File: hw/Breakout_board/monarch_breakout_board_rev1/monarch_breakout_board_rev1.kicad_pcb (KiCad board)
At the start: 2 copper layers, 21 x 21 mm, 19 parts, among them J108 Conn_01x03, J14 5037630491, U2 FDC2214RGHR, U3 INA226AQDGSRQ1, U4 INA226AQDGSRQ1

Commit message: Footprints, Connectors, and Routing
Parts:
- removed J108: Conn_01x03, Connector_PinSocket_2.54mm:PinSocket_1x03_P2.54mm_Vertical
- removed J14: 5037630491, Connector 4 Pin:CONN_5037630000-SD_04_MOL
- added J1: 5037630491, Connector 4 Pin:CONN_5037630000-SD_04_MOL, F.Cu at (91.7, 36.2)
- added J2: 5037630291, Connector 2 Pin:CONN_5037630000-SD_02_MOL, F.Cu at (83.1, 32.2)
- added J3: 5037630291, Connector 2 Pin:CONN_5037630000-SD_02_MOL, F.Cu at (84.7, 49.5)
- added J4: 5037630291, Connector 2 Pin:CONN_5037630000-SD_02_MOL, F.Cu at (76.8, 49.5)
- added J5: 5037630291, Connector 2 Pin:CONN_5037630000-SD_02_MOL, F.Cu at (74.7, 41.9)
- added J6: 5037630291, Connector 2 Pin:CONN_5037630000-SD_02_MOL, F.Cu at (91.7, 45.0)
- added L1: 18uH, Inductor_SMD:L_0805_2012Metric, F.Cu at (111.0, 50.7)
- added L2: 18uH, Inductor_SMD:L_0805_2012Metric, F.Cu at (111.0, 47.1)
- added L5: 18uH, Inductor_SMD:L_0805_2012Metric, F.Cu at (104.8, 52.1)
- added L6: 18uH, Inductor_SMD:L_0805_2012Metric, F.Cu at (108.4, 52.1)
- added TP5: TestPoint, TestPoint:TestPoint_2Pads_Pitch2.54mm_Drill0.8mm, F.Cu at (106.9, 22.6)
- added TP6: TestPoint, TestPoint:TestPoint_2Pads_Pitch2.54mm_Drill0.8mm, F.Cu at (106.9, 25.9)
- added TP7: TestPoint, TestPoint:TestPoint_2Pads_Pitch2.54mm_Drill0.8mm, F.Cu at (106.9, 29.3)
- added TP8: TestPoint, TestPoint:TestPoint_2Pads_Pitch2.54mm_Drill0.8mm, F.Cu at (106.8, 29.5)
- moved C2 58.3 mm to (113.0, 50.5), turned to 90 degrees
- moved C5 54.3 mm to (113.0, 47.2), turned to 90 degrees
- moved C1 50.9 mm to (103.2, 50.2), turned to 180 degrees
- moved C10 49.3 mm to (108.4, 53.8)
- moved C9 48.1 mm to (104.8, 53.8)
- moved C3 48.1 mm to (104.1, 47.9), turned to -90 degrees
- moved R122 44.2 mm to (108.8, 45.8), turned to 180 degrees
- moved C8 44.2 mm to (102.3, 47.9), turned to -90 degrees
- moved R117 43.8 mm to (107.3, 45.3), turned to -90 degrees
- moved C4 43.3 mm to (100.5, 47.8), turned to -90 degrees
- moved U2 26.9 mm to (107.5, 48.8), turned to -90 degrees
- moved D104 17.9 mm to (91.7, 30.4), turned to 180 degrees
- moved R141 16.1 mm to (88.8, 30.4)
- moved R2 12.2 mm to (77.3, 30.6), turned to 0 degrees
- moved R3 8.94 mm to (87.5, 34.5)
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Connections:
- U2 pad 4: unconnected-(U2-ADDR-Pad4) -> GND
- U3 pad 1: unconnected-(U3-A1-Pad1) -> GND
- U3 pad 2: unconnected-(U3-A0-Pad2) -> GND
- U4 pad 1: unconnected-(U4-A1-Pad1) -> GND
- U4 pad 2: unconnected-(U4-A0-Pad2) -> +3.3V
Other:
- board size 21 x 21 mm -> 23 x 23 mm
- board text added: "Look at application circuit in the datasheet... will be much better"

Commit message: Breakout Board History Fix
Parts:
- added H1: MountingHole, MountingHole:MountingHole_2.2mm_M2_DIN965_Pad, F.Cu at (118.0, 32.6)
- added H2: MountingHole, MountingHole:MountingHole_2.2mm_M2_DIN965_Pad, F.Cu at (118.0, 55.5)
- added H3: MountingHole, MountingHole:MountingHole_2.2mm_M2_DIN965_Pad, F.Cu at (96.8, 32.7)
- added H4: MountingHole, MountingHole:MountingHole_2.2mm_M2_DIN965_Pad, F.Cu at (96.5, 55.7)
- added Y1: SiT5000AI-2E-33N0-40, Oscillator:Oscillator_SMD_SiT_PQFN-4Pin_3.2x2.5mm, F.Cu at (102.8, 44.6)
- moved J5 42.8 mm to (117.4, 40.1), turned to -90 degrees
- moved J4 40.6 mm to (117.4, 47.9), turned to -90 degrees
- moved J3 31.7 mm to (111.6, 32.8), turned to 0 degrees
- moved R122 29.5 mm to (81.0, 35.9)
- moved R141 29.2 mm to (110.8, 49.6), turned to 90 degrees
- moved D104 28.3 mm to (112.2, 49.9), turned to 90 degrees
- moved R117 27.7 mm to (82.2, 33.6), turned to 0 degrees
- moved J1 25.8 mm to (109.3, 55.1), turned to 180 degrees
- moved U3 23.4 mm to (100.4, 38.2), turned to 180 degrees
- moved R3 22.8 mm to (65.4, 29.2), turned to 0 degrees
- moved U4 21.2 mm to (101.7, 53.6)
- moved R2 21.2 mm to (56.1, 29.2)
- moved J2 19.3 mm to (96.9, 45.6), turned to 90 degrees
- moved J6 17.2 mm to (103.7, 32.8), turned to 0 degrees
- moved TP5 14.0 mm to (120.4, 18.6)
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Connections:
- C10 pad 1: /Cap3+ -> Cap3+
- C10 pad 2: /Cap4- -> Cap4-
- C2 pad 1: /Cap5+ -> Cap5+
- C2 pad 2: /Cap6- -> Cap6-
- C5 pad 1: /Cap7+ -> Cap7+
- C5 pad 2: /Cap8- -> Cap8-
- C9 pad 1: /Cap1+ -> Cap1+
- C9 pad 2: /Cap2- -> Cap2-
- J1 pad 1: /Connectors/I2C4_SDA -> I2C4_SDA
- J1 pad 2: /Connectors/I2C4_SCL -> I2C4_SCL
- J2 pad 1: /Connectors/Electro1 -> Electro1
- J2 pad 2: /Connectors/Electro2 -> Electro2
- J3 pad 1: /Connectors/Cap5+ -> Cap5+
- J3 pad 2: /Connectors/Cap6- -> Cap6-
- J4 pad 1: /Connectors/Cap1+ -> Cap1+
- J4 pad 2: /Connectors/Cap2- -> Cap2-
- J5 pad 1: /Connectors/Cap3+ -> Cap3+
- J5 pad 2: /Connectors/Cap4- -> Cap4-
- J6 pad 1: /Connectors/Cap7+ -> Cap7+
- J6 pad 2: /Connectors/Cap8- -> Cap8-
- L1 pad 1: /Cap5+ -> Cap5+
- L1 pad 2: /Cap6- -> Cap6-
- L2 pad 1: /Cap7+ -> Cap7+
- L2 pad 2: /Cap8- -> Cap8-
- L5 pad 1: /Cap1+ -> Cap1+
- L5 pad 2: /Cap2- -> Cap2-
- L6 pad 1: /Cap3+ -> Cap3+
- L6 pad 2: /Cap4- -> Cap4-
- R117 pad 2: /I2C4_SDA -> I2C4_SDA
- R122 pad 2: /I2C4_SCL -> I2C4_SCL
- R2 pad 1: /Electro1 -> Electro1
- R3 pad 1: /Electro2 -> Electro2
- TP5 pad 1: /Connectors/I2C4_SCL -> I2C4_SCL
- TP7 pad 1: /Connectors/I2C4_SDA -> I2C4_SDA
- U2 pad 1: /I2C4_SCL -> I2C4_SCL
- U2 pad 10: /Cap2- -> Cap2-
- U2 pad 11: /Cap3+ -> Cap3+
- U2 pad 12: /Cap4- -> Cap4-
- U2 pad 13: /Cap5+ -> Cap5+
- U2 pad 14: /Cap6- -> Cap6-
- U2 pad 15: /Cap7+ -> Cap7+
- U2 pad 16: /Cap8- -> Cap8-
- U2 pad 2: /I2C4_SDA -> I2C4_SDA
- U2 pad 3: unconnected-(U2-CLKIN-Pad3) -> /CLK_40MHz
- U2 pad 9: /Cap1+ -> Cap1+
- U3 pad 10: /Electro1 -> Electro1
- U3 pad 4: /I2C4_SDA -> I2C4_SDA
- U3 pad 5: /I2C4_SCL -> I2C4_SCL
- U3 pad 8: /Electro1 -> Electro1
- U4 pad 10: /Electro2 -> Electro2
- U4 pad 4: /I2C4_SDA -> I2C4_SDA
- U4 pad 5: /I2C4_SCL -> I2C4_SCL
- U4 pad 8: /Electro2 -> Electro2
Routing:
- net Cap1+: track 0.00 -> 8.76 mm
- net Cap5+: track 0.00 -> 8.55 mm
- net Cap8-: track 0.00 -> 7.84 mm
- net Cap2-: track 0.00 -> 7.76 mm
- net Cap6-: track 0.00 -> 7.37 mm
- net Cap7+: track 0.00 -> 7.26 mm
- net Cap4-: track 0.00 -> 7.09 mm
- net Cap3+: track 0.00 -> 6.63 mm
- net +3V3: track 0.00 -> 2.52 mm
- net /CLK_40MHz: track 0.00 -> 2.06 mm
- net +3.3V: track 0.00 -> 1.69 mm
- net Net-(D104-A): track 0.00 -> 1.50 mm
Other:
- board text removed: "Look at application circuit in the datasheet... will be much better"

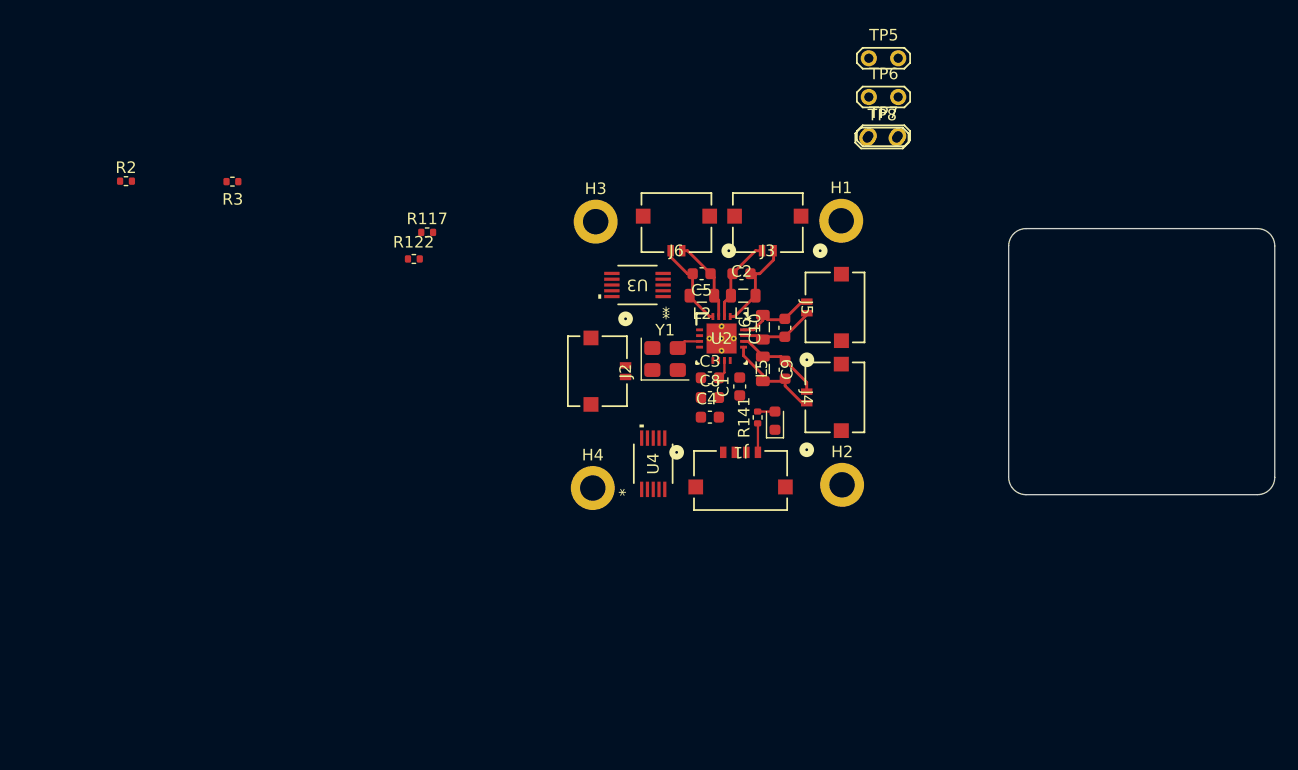
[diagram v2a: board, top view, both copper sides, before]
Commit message: Amplifier Initial Setup / Routing Work
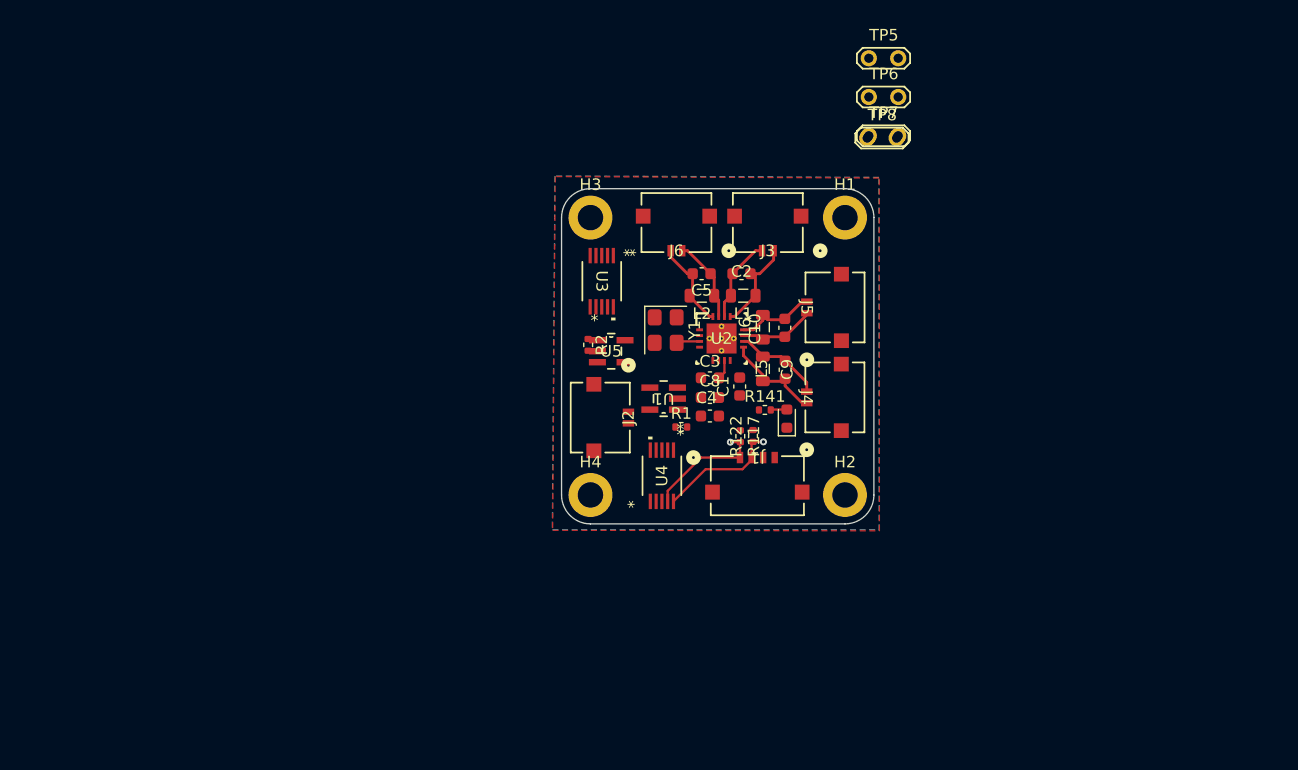
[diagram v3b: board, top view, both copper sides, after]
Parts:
- removed R3: ?, Resistor_SMD:R_0402_1005Metric
- added R1: ?, Resistor_SMD:R_0402_1005Metric, F.Cu at (104.2, 50.5)
- added U1: OPA320AIDBVR, OPA320:DBV5, F.Cu at (102.6, 48.0)
- added U5: OPA320AIDBVR, OPA320:DBV5, F.Cu at (98.1, 43.9)
- moved R2 42.4 mm to (96.1, 43.4), turned to -90 degrees
- moved R122 33.1 mm to (110.3, 51.2), turned to -90 degrees
- moved R117 32.3 mm to (109.2, 51.2), turned to -90 degrees
- moved J2 4.02 mm to (97.1, 49.6)
- moved U3 3.11 mm to (97.3, 37.9), turned to -90 degrees
- moved Y1 2.50 mm to (102.8, 42.1), turned to -90 degrees
- moved J1 1.52 mm to (110.7, 55.5)
- moved U4 1.28 mm to (102.5, 54.7)
- moved D104 1.04 mm to (113.3, 49.7)
- moved H2 0.91 mm to (118.3, 56.3)
- moved R141 0.90 mm to (111.4, 49.0), turned to 0 degrees
- moved H4 0.63 mm to (96.3, 56.3)
- moved H3 0.57 mm to (96.3, 32.4)
- moved H1 0.43 mm to (118.3, 32.4)
- moved C4 0.10 mm to (106.6, 49.5)
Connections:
- R2 pad 1: Electro1 -> unconnected-(R2-Pad1)
- R2 pad 2: GND -> unconnected-(R2-Pad2)
- U3 pad 10: Electro1 -> /VBUS_1
- U3 pad 8: Electro1 -> /VBUS_1
- U3 pad 9: GND -> /VIN-_1
- U4 pad 10: Electro2 -> /VIN+_2
- U4 pad 8: Electro2 -> /VBUS_2
- U4 pad 9: GND -> /VIN-_2
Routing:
- net I2C4_SCL: track 0.00 -> 11.2 mm, vias 0 -> 1
- net I2C4_SDA: track 0.00 -> 10.6 mm, vias 0 -> 1
- net +3V3: track 2.52 -> 0.00 mm
- added copper zone on B.Cu, net GND
- added copper zone on F.Cu, net GND
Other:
- board size 23 x 23 mm -> 27 x 29 mm

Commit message: Final Breakout Board Work
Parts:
- removed C4, C8: 0.01 uF, Capacitor_SMD:C_0603_1608Metric
- removed J1: 5037630491, Connector 4 Pin:CONN_5037630000-SD_04_MOL
- removed R1, R2: ?, Resistor_SMD:R_0402_1005Metric
- removed R117, R122: 4.7k, Resistor_SMD:R_0402_1005Metric
- removed U1, U5: OPA320AIDBVR, OPA320:DBV5
- removed U3, U4: INA226AQDGSRQ1, INA226-Q1:DGS10_TEX
- removed Y1: SiT5000AI-2E-33N0-40, Oscillator:Oscillator_SMD_SiT_PQFN-4Pin_3.2x2.5mm
- J2: value 5037630291 -> 5037630491; footprint Connector 2 Pin:CONN_5037630000-SD_02_MOL -> Connector 4 Pin:CONN_5037630000-SD_04_MOL
- TP5, TP6, TP7, TP8: footprint TestPoint:TestPoint_2Pads_Pitch2.54mm_Drill0.8mm -> TestPoint:TestPoint_Keystone_5000-5004_Miniature
- moved TP5 39.7 mm to (116.5, 58.1), turned to 180 degrees
- moved TP8 35.5 mm to (109.3, 59.3), turned to 180 degrees
- moved TP6 35.5 mm to (109.3, 55.6), turned to 180 degrees
- moved H3 34.0 mm to (109.4, 63.7), turned to 90 degrees
- moved TP7 33.8 mm to (113.1, 58.3), turned to 180 degrees
- moved H4 31.9 mm to (127.4, 63.6), turned to 90 degrees
- moved J2 25.4 mm to (118.7, 63.0), turned to 180 degrees
- moved H2 17.3 mm to (127.4, 41.6), turned to 90 degrees
- moved J6 16.1 mm to (109.7, 47.8), turned to 90 degrees
- moved D104 14.0 mm to (112.6, 63.7)
- moved C1 13.4 mm to (119.0, 56.1)
- moved C3 13.3 mm to (116.4, 55.2)
- moved C10 13.1 mm to (122.8, 50.6)
- moved C2 13.1 mm to (119.1, 45.9)
- moved C9 13.1 mm to (122.9, 54.2)
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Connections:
- C1 pad 2: +3.3V -> +3V3
- C3 pad 2: +3.3V -> +3V3
- J2 pad 1: Electro1 -> I2C4_SDA
- J2 pad 2: Electro2 -> I2C4_SCL
- J2 pad 3: (no net) -> GND
- J2 pad 4: (no net) -> +3V3
- U2 pad 3: /CLK_40MHz -> unconnected-(U2-CLKIN-Pad3)
- U2 pad 7: +3.3V -> +3V3
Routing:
- net +3V3: track 0.00 -> 25.0 mm, vias 0 -> 2
- net I2C4_SDA: track 10.6 -> 14.2 mm
- net Cap8-: track 7.84 -> 5.27 mm
- net /CLK_40MHz: track 2.03 -> 0.00 mm
- net I2C4_SCL: track 11.2 -> 13.2 mm, vias 1 -> 0
- net Cap5+: track 8.55 -> 6.59 mm
- net Cap6-: track 7.37 -> 5.60 mm
- net +3.3V: track 1.69 -> 0.00 mm
- net Cap7+: track 7.26 -> 7.96 mm
- net Cap3+: track 6.63 -> 7.13 mm
- net GND: vias 0 -> 9
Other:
- board size 27 x 29 mm -> 23 x 27.1 mm

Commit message: Breakout Board DONE
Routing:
- net GND: track 0.00 -> 3.49 mm, vias 9 -> 12
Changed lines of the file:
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@@
 		)
 		(embedded_fonts no)
+		(model "${KIPRJMOD}/5037630491/5037630491.stp"
+			(offset
+				(xyz -1.5 4.5 0)
+			)
+			(scale
+				(xyz 1 1 1)
+			)
+			(rotate
+				(xyz -0 -0 -180)
+			)
+		)
 	)
 	(footprint "Capacitor_SMD:C_0603_1608Metric"
@@
 		)
 		(embedded_fonts no)
+		(model "${KIPRJMOD}/5037630291/5037630291.stp"
+			(offset
+				(xyz -0.5 4.5 0)
+			)
+			(scale
+				(xyz 1 1 1)
+			)
+			(rotate
+				(xyz -0 -0 -180)
+			)
+		)
 	)
 	(footprint "FDC2214:RGH0016A"
@@
 		)
 		(embedded_fonts no)
+		(model "${KIPRJMOD}/FDC2214/RGH0016A.stp"
+			(offset
+				(xyz 0 0 0)
+			)
+			(scale
+				(xyz 1 1 1)
+			)
+			(rotate
+				(xyz 0 0 0)
+			)
+		)
 	)
 	(footprint "Capacitor_SMD:C_0603_1608Metric"
@@
 		)
 		(embedded_fonts no)
+		(model "${KIPRJMOD}/5037630291/5037630291.stp"
+			(offset
+				(xyz -0.5 4.5 0)
+			)
+			(scale
+				(xyz 1 1 1)
+			)
+			(rotate
+				(xyz -0 -0 -180)
+			)
+		)
 	)
 	(footprint "Capacitor_SMD:C_0603_1608Metric"
@@
 		)
 		(embedded_fonts no)
+		(model "${KIPRJMOD}/5037630291/5037630291.stp"
+			(offset
+				(xyz -0.5 4.5 0)
+			)
+			(scale
+				(xyz 1 1 1)
+			)
+			(rotate
+				(xyz -0 -0 -180)
+			)
+		)
 	)
 	(footprint "Connector 2 Pin:CONN_5037630000-SD_02_MOL"
@@
 		)
 		(embedded_fonts no)
+		(model "${KIPRJMOD}/5037630291/5037630291.stp"
+			(offset
+				(xyz -0.5 4.5 0)
+			)
+			(scale
+				(xyz 1 1 1)
+			)
+			(rotate
+				(xyz -0 -0 -180)
+			)
+		)
 	)
 	(gr_line
@@
 		(layer "Edge.Cuts")
 	)
+	(segment
+		(start 115.462503 53.162497)
+		(end 115.45 53.175)
+		(width 0.2)
+		(layer "F.Cu")
+		(net 1)
+	)
+	(segment
+		(start 115.462503 52.249999)
+		(end 115.462503 53.162497)
+		(width 0.2)
+		(layer "F.Cu")
+		(net 1)
+	)
+	(segment
+		(start 116.612501 52.249999)
+		(end 116.972887 51.889613)
+		(width 0.2)
+		(layer "F.Cu")
+		(net 1)
+	)
+	(segment
+		(start 118.112503 53.437503)
+		(end 118.725 54.05)
+		(width 0.2)
+		(layer "F.Cu")
+		(net 1)
+	)
+	(segment
+		(start 115.462503 52.249999)
+		(end 116.612501 52.249999)
+		(width 0.2)
+		(layer "F.Cu")
+		(net 1)
+	)
+	(segment
+		(start 118.112503 53.4)
+		(end 118.112503 53.437503)
+		(width 0.2)
+		(layer "F.Cu")
+		(net 1)
+	)
 	(via
 		(at 111.7 52.55)
@@
 	)
 	(via
+		(at 117.362502 51.499998)
+		(size 0.6)
+		(drill 0.3)
+		(layers "F.Cu" "B.Cu")
+		(net 1)
+	)
+	(via
 		(at 113.725 49.7)
 		(size 0.6)
@@
 	)
 	(via
+		(at 117.362502 51.499998)
+		(size 0.6)
+		(drill 0.3)
+		(layers "F.Cu" "B.Cu")
+		(net 1)
+	)
+	(via
 		(at 119.2 59.4)
 		(size 0.6)
@@
 		(net 1)
 	)
+	(via
+		(at 118.725 54.05)
+		(size 0.6)
+		(drill 0.3)
+		(layers "F.Cu" "B.Cu")
+		(free yes)
+		(net 1)
+	)
 	(segment
 		(start 112.635 61.9075)
@@
 	)
 	(zone
+		(net 1)
+		(net_name "GND")
+		(layer "F.Cu")
+		(hatch edge 0.5)
+		(priority 2)
+		(connect_pads
+			(clearance 0)
+		)
+		(min_thickness 0.25)
+		(filled_areas_thickness no)
+		(fill yes
+			(thermal_gap 0.5)
+			(thermal_bridge_width 0.5)
+		)
+		(polygon
+			(pts
+				(xy 118.6 52.8) (xy 118.6 50.25) (xy 116.075 50.25) (xy 116.1 52.75) (xy 118.625 52.775)
+			)
+		)
+	)
+	(zone

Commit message: FIXES after Review
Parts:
- removed J5, J6: 5037630291, Connector 2 Pin:CONN_5037630000-SD_02_MOL
- C6: renamed from C3; value 0.01 uF -> 0.1 uF
- D1: renamed from D104; footprint LED_SMD:LED_0603_1608Metric -> LED_SMD:LED_0603_1608Metric_Pad1.05x0.95mm_HandSolder
- J2: renamed from J4; value 5037630291 -> 5037630491; footprint Connector 2 Pin:CONN_5037630000-SD_02_MOL -> Connector 4 Pin:CONN_5037630000-SD_04_MOL
- J3: value 5037630291 -> 5037630491; footprint Connector 2 Pin:CONN_5037630000-SD_02_MOL -> Connector 4 Pin:CONN_5037630000-SD_04_MOL
- R1: renamed from R141; value 470 -> 100; footprint Resistor_SMD:R_0402_1005Metric -> Resistor_SMD:R_0201_0603Metric_Pad0.64x0.40mm_HandSolder
- moved TP2 20.5 mm to (127.3, 45.8)
- moved TP4 17.9 mm to (127.2, 59.5)
- moved TP1 12.3 mm to (109.2, 48.3)
- moved TP3 7.59 mm to (109.2, 51.8)
- moved D1 5.65 mm to (109.3, 59.1), turned to 0 degrees
- moved C5 3.89 mm to (115.4, 57.7), turned to 0 degrees
- moved J2 3.63 mm to (126.6, 52.6)
- moved C3 3.16 mm to (117.8, 48.8)
- moved J3 2.14 mm to (117.0, 42.5)
- moved R1 2.05 mm to (112.0, 59.2), turned to 180 degrees
- moved U1 1.84 mm to (116.0, 52.7)
- moved C4 1.67 mm to (114.6, 48.8), turned to 180 degrees
- moved C6 1.34 mm to (115.4, 56.2)
- moved L3 1.31 mm to (118.1, 46.9)
- moved L4 1.13 mm to (114.3, 46.9), turned to 180 degrees
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- renumbered C9 to C1, C10 to C2, C2 to C3, C5 to C4, C1 to C5, H3 to H2, H2 to H3, J2 to J1, L5 to L1, L6 to L2, L1 to L3, L2 to L4, TP5 to TP1, TP6 to TP2, TP7 to TP3, TP8 to TP4, U2 to U1
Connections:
- net Cap5+ renamed Cap2+
- C1 pad 1: Cap1+ -> Cap0+
- C1 pad 2: Cap2- -> Cap0-
- C2 pad 1: Cap3+ -> Cap1+
- C2 pad 2: Cap4- -> Cap1-
- C3 pad 2: Cap6- -> Cap2-
- C4 pad 1: Cap7+ -> Cap3+
- C4 pad 2: Cap8- -> Cap3-
- J2 pad 1: Cap1+ -> Cap0+
- J2 pad 2: Cap2- -> Cap0-
- J2 pad 3: (no net) -> Cap1+
- J2 pad 4: (no net) -> Cap1-
- J3 pad 2: Cap6- -> Cap2-
- J3 pad 3: (no net) -> Cap3+
- J3 pad 4: (no net) -> Cap3-
- L1 pad 1: Cap1+ -> Cap0+
- L1 pad 2: Cap2- -> Cap0-
- L2 pad 1: Cap3+ -> Cap1+
- L2 pad 2: Cap4- -> Cap1-
- L3 pad 2: Cap6- -> Cap2-
- L4 pad 1: Cap7+ -> Cap3+
- L4 pad 2: Cap8- -> Cap3-
- U1 pad 10: Cap2- -> Cap0-
- U1 pad 11: Cap3+ -> Cap1+
- U1 pad 12: Cap4- -> Cap1-
- U1 pad 14: Cap6- -> Cap2-
- U1 pad 15: Cap7+ -> Cap3+
- U1 pad 16: Cap8- -> Cap3-
- U1 pad 9: Cap1+ -> Cap0+
- U1 pad V: (no net) -> GND
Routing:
- net GND: track 3.49 -> 12.3 mm, vias 12 -> 5
- net Cap0+: track 0.00 -> 8.16 mm
- net Cap7+: track 7.96 -> 0.00 mm
- net Cap3-: track 0.00 -> 7.92 mm
- net Cap1-: track 0.00 -> 7.66 mm
- net Cap4-: track 7.35 -> 0.00 mm
- net Cap0-: track 0.00 -> 6.65 mm
- net Cap6-: track 5.60 -> 0.00 mm
- net Cap8-: track 5.27 -> 0.00 mm
- net I2C4_SCL: track 13.2 -> 17.5 mm, vias 0 -> 2
- net +3V3: track 25.0 -> 21.0 mm, vias 2 -> 0
- net Cap1+: track 8.58 -> 6.53 mm
- net Cap2-: track 7.84 -> 6.34 mm
- net I2C4_SDA: track 14.2 -> 15.5 mm, vias 1 -> 2
- net Cap3+: track 7.13 -> 6.39 mm
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- removed copper zone on F.Cu, net GND

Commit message: FIXES V2
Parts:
- R1: footprint Resistor_SMD:R_0201_0603Metric_Pad0.64x0.40mm_HandSolder -> Resistor_SMD:R_0603_1608Metric_Pad0.98x0.95mm_HandSolder
- moved R1 3.06 mm to (109.3, 60.7)
- moved D1 1.35 mm to (108.4, 58.1), turned to -90 degrees
- moved J1 0.63 mm to (118.1, 63.5)
- moved J2 0.63 mm to (127.2, 52.7)
- moved J3 0.58 mm to (117.0, 42.0)
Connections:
- J1 pad 1: I2C4_SDA -> +3V3
- J1 pad 2: I2C4_SCL -> GND
- J1 pad 3: GND -> I2C4_SCL
- J1 pad 4: +3V3 -> I2C4_SDA
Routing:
- net +3V3: track 21.0 -> 27.1 mm
- net I2C4_SDA: track 15.5 -> 18.5 mm
- net I2C4_SCL: track 17.5 -> 19.3 mm
- net GND: track 12.3 -> 12.8 mm
